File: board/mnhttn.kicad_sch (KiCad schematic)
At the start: 10 parts, among them SW1 SW_Push, SW2 SW_SPDT, SW3 SW_Push, SW4 SW_SPDT, U1 xiao-ble, U2 xiao-ble

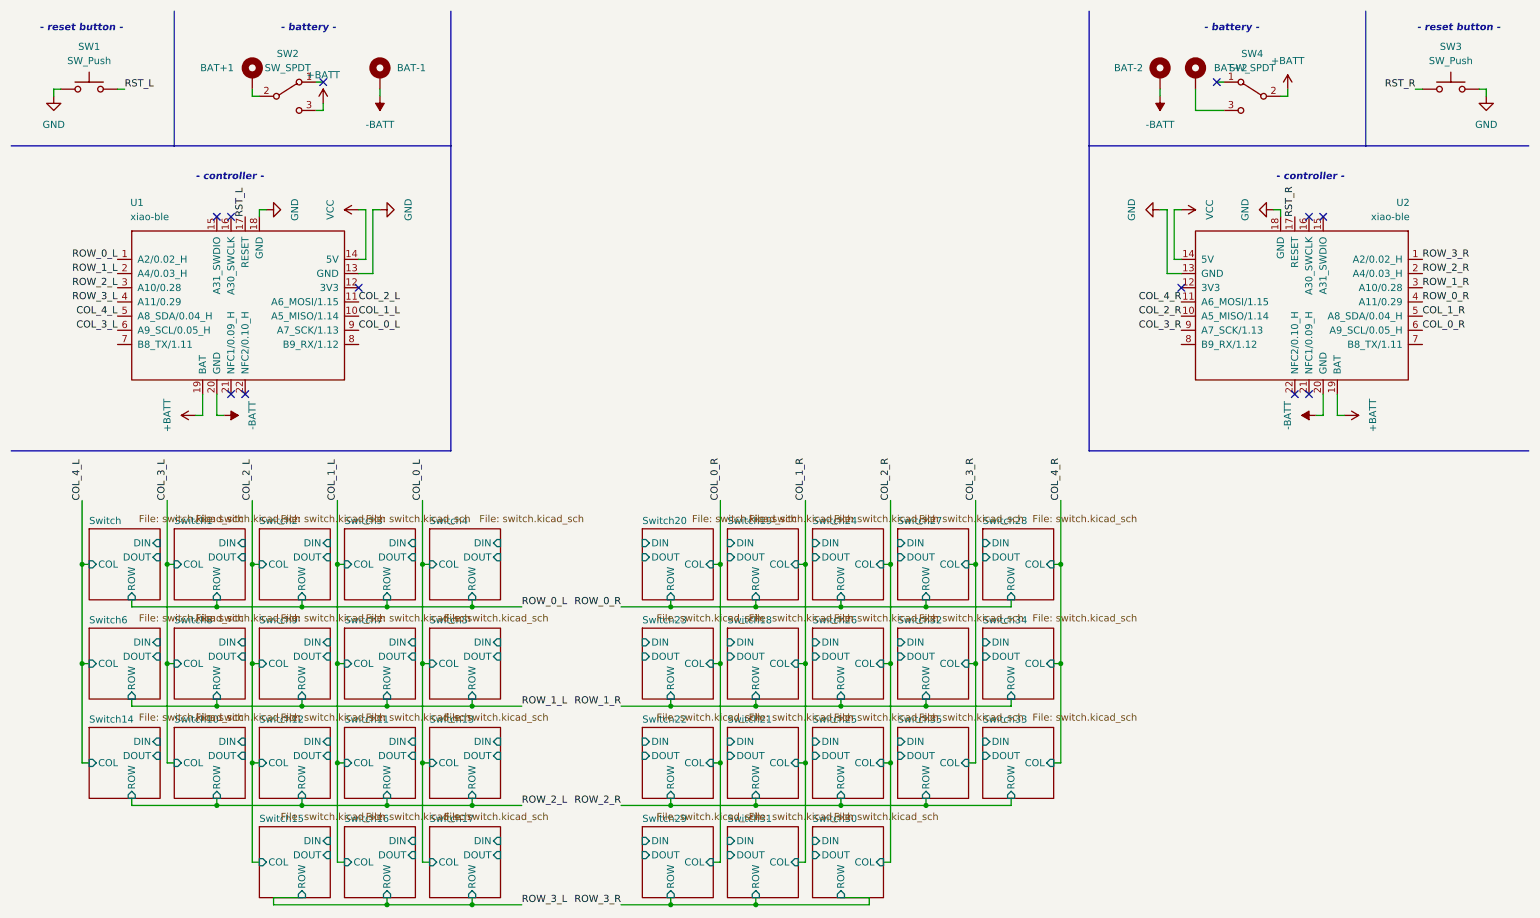
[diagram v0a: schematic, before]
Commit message: changed to 5*4+3+1 layout
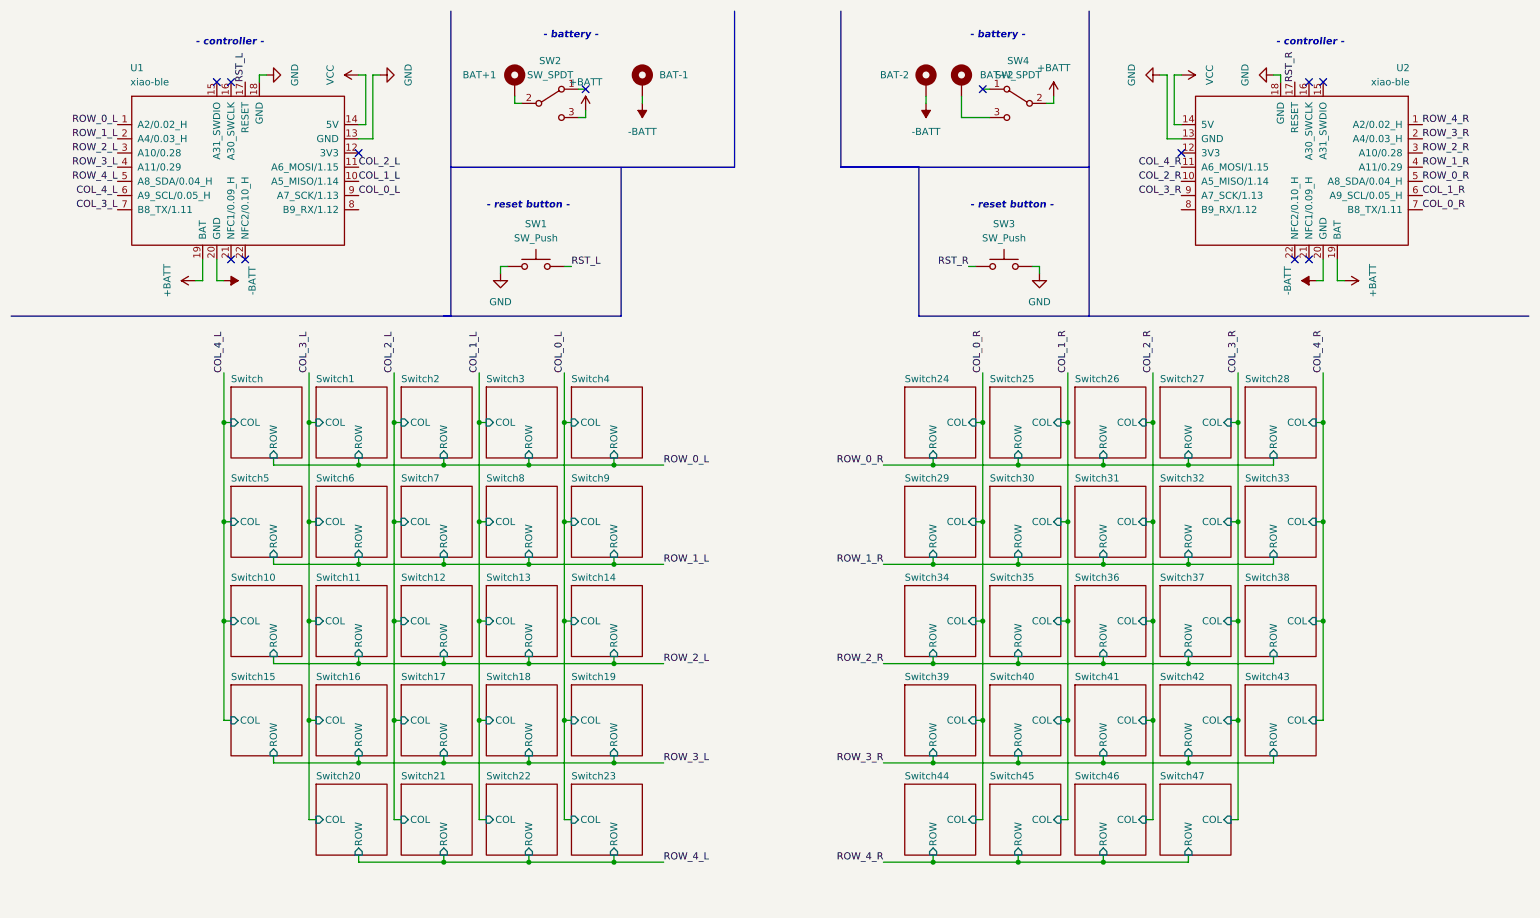
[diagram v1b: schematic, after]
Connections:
- net COL_0_R: now also U2.7 (B8_TX/1.11); no longer U2.6 (A9_SCL/0.05_H)
- net COL_1_R: now also U2.6 (A9_SCL/0.05_H); no longer U2.5 (A8_SDA/0.04_H)
- net COL_3_L: now also U1.7 (B8_TX/1.11); no longer U1.6 (A9_SCL/0.05_H)
- net COL_4_L: now also U1.6 (A9_SCL/0.05_H); no longer U1.5 (A8_SDA/0.04_H)
- net ROW_0_R: now also U2.5 (A8_SDA/0.04_H); no longer U2.4 (A11/0.29)
- net ROW_1_R: now also U2.4 (A11/0.29); no longer U2.3 (A10/0.28)
- net ROW_2_R: now also U2.3 (A10/0.28); no longer U2.2 (A4/0.03_H)
- net ROW_3_R: now also U2.2 (A4/0.03_H); no longer U2.1 (A2/0.02_H)
- new net ROW_4_L: U1.5 (A8_SDA/0.04_H)
- new net ROW_4_R: U2.1 (A2/0.02_H)
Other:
- added sheet Switch36 (switch.kicad_sch)
- added sheet Switch37 (switch.kicad_sch)
- added sheet Switch38 (switch.kicad_sch)
- added sheet Switch39 (switch.kicad_sch)
- added sheet Switch40 (switch.kicad_sch)
- added sheet Switch41 (switch.kicad_sch)
- added sheet Switch42 (switch.kicad_sch)
- added sheet Switch43 (switch.kicad_sch)
- added sheet Switch44 (switch.kicad_sch)
- added sheet Switch45 (switch.kicad_sch)
- added sheet Switch46 (switch.kicad_sch)
- added sheet Switch47 (switch.kicad_sch)
- sheet Switch ports: added none; removed DIN, DOUT
- sheet Switch1 ports: added none; removed DIN, DOUT
- sheet Switch10 ports: added none; removed DIN, DOUT
- sheet Switch11 ports: added none; removed DIN, DOUT
- sheet Switch12 ports: added none; removed DIN, DOUT
- sheet Switch13 ports: added none; removed DIN, DOUT
- sheet Switch14 ports: added none; removed DIN, DOUT
- sheet Switch15 ports: added none; removed DIN, DOUT
- sheet Switch16 ports: added none; removed DIN, DOUT
- sheet Switch17 ports: added none; removed DIN, DOUT
- sheet Switch18 ports: added none; removed DIN, DOUT
- sheet Switch19 ports: added none; removed DIN, DOUT
- sheet Switch2 ports: added none; removed DIN, DOUT
- sheet Switch20 ports: added none; removed DIN, DOUT
- sheet Switch21 ports: added none; removed DIN, DOUT
- sheet Switch22 ports: added none; removed DIN, DOUT
- sheet Switch23 ports: added none; removed DIN, DOUT
- sheet Switch24 ports: added none; removed DIN, DOUT
- sheet Switch25 ports: added none; removed DIN, DOUT
- sheet Switch26 ports: added none; removed DIN, DOUT
- sheet Switch27 ports: added none; removed DIN, DOUT
- sheet Switch28 ports: added none; removed DIN, DOUT
- sheet Switch29 ports: added none; removed DIN, DOUT
- sheet Switch3 ports: added none; removed DIN, DOUT
- sheet Switch30 ports: added none; removed DIN, DOUT
- sheet Switch31 ports: added none; removed DIN, DOUT
- sheet Switch32 ports: added none; removed DIN, DOUT
- sheet Switch33 ports: added none; removed DIN, DOUT
- sheet Switch34 ports: added none; removed DIN, DOUT
- sheet Switch35 ports: added none; removed DIN, DOUT
- sheet Switch4 ports: added none; removed DIN, DOUT
- sheet Switch5 ports: added none; removed DIN, DOUT
- sheet Switch6 ports: added none; removed DIN, DOUT
- sheet Switch7 ports: added none; removed DIN, DOUT
- sheet Switch8 ports: added none; removed DIN, DOUT
- sheet Switch9 ports: added none; removed DIN, DOUT
- moved on the sheet: U1, U2
